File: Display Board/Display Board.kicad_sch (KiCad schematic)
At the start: 12 parts, among them J1 Display 1, J10 Display 1, J2 Display 2, J20 Display 2, J3 Control Board, J4 Top LED

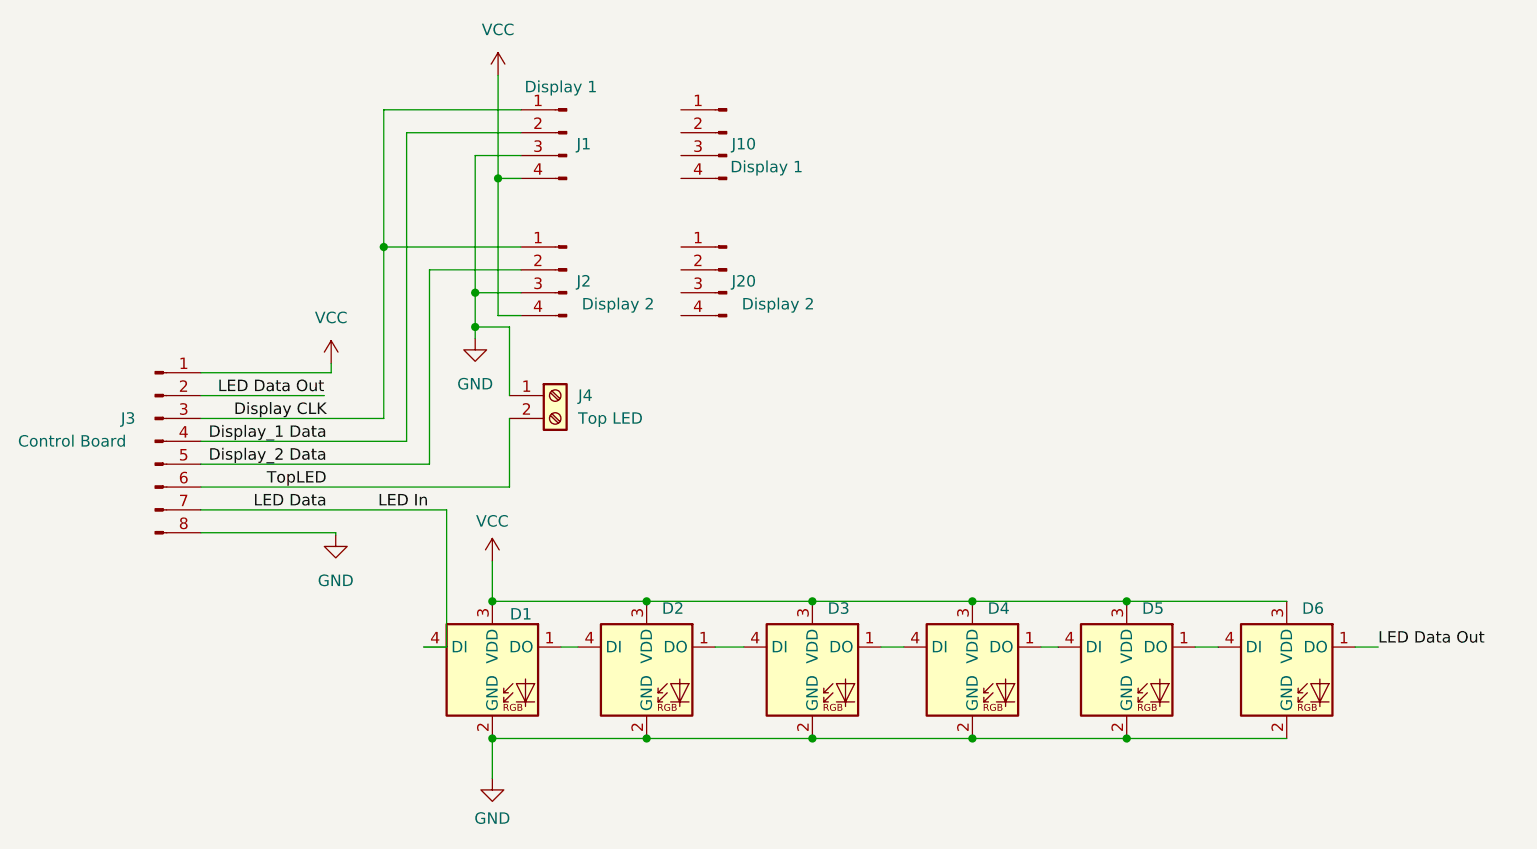
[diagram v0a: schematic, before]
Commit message: working on display board and mounting
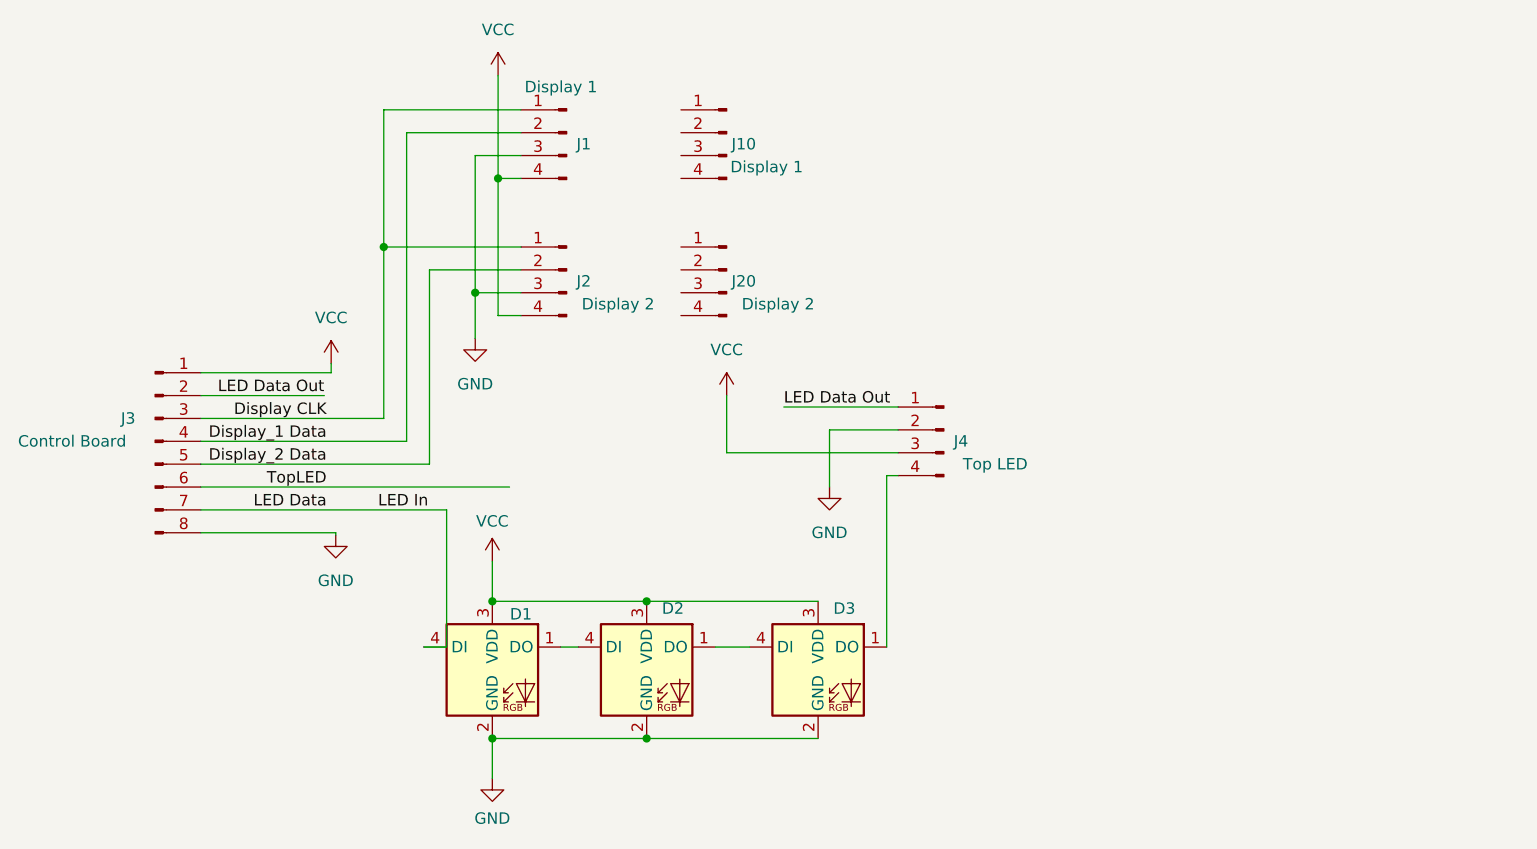
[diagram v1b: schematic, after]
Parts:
- removed D4, D5, D6: APA-106-F5, LED_THT:LED_D5.0mm-4_RGB, symbol LED:APA-106-F5
- removed J4: Top LED, TerminalBlock:TerminalBlock_Altech_AK300-2_P5.00mm, symbol Connector:Screw_Terminal_01x02
- added J4: Top LED, Connector_PinHeader_2.00mm:PinHeader_1x04_P2.00mm_Vertical, symbol Connector:Conn_01x04_Pin
- J1, J10, J2, J20: footprint Connector_PinHeader_2.00mm:PinHeader_1x04_P2.00mm_Vertical -> Connector_PinHeader_2.54mm:PinHeader_1x04_P2.54mm_Vertical
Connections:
- net GND: now also J4.2 (Pin_2)
- net LED Data Out: now also J4.1 (Pin_1)
- net VCC: now also J4.3 (Pin_3)
- net at D3.1 (DO): now also J4.4 (Pin_4)
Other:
- moved on the sheet: D3

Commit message: update display board with mounting holes and copper pour
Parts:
- added J5: Flash Enable, Connector_PinHeader_2.54mm:PinHeader_1x02_P2.54mm_Vertical, symbol Connector_Generic:Conn_01x02
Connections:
- net Display_1 Data: now also J5.2 (Pin_2); no longer J1.2 (Pin_2)
- new net: J1.2 (Pin_2), J5.1 (Pin_1)
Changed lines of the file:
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@@
+    (stroke (width 0) (type default))
+  )
+  (wire (pts (xy 69.85 34.29) (xy 76.2 34.29))
     (stroke (width 0) (type default))
   )
@@
     (stroke (width 0) (type default))
   )
-  (wire (pts (xy 76.2 66.04) (xy 76.2 31.75))
-    (stroke (width 0) (type default))
-  )
   (wire (pts (xy 88.9 49.53) (xy 83.82 49.53))
     (stroke (width 0) (type default))
@@
     (stroke (width 0) (type default))
   )
+  (wire (pts (xy 76.2 66.04) (xy 76.2 34.29))
+    (stroke (width 0) (type default))
+  )
   (wire (pts (xy 73.66 44.45) (xy 73.66 29.21))
     (stroke (width 0) (type default))
@@
     (stroke (width 0) (type default))
   )
-  (wire (pts (xy 76.2 31.75) (xy 88.9 31.75))
+  (wire (pts (xy 69.85 31.75) (xy 88.9 31.75))
     (stroke (width 0) (type default))
   )
@@
   (wire (pts (xy 93.345 88.9) (xy 95.25 88.9))
     (stroke (width 0) (type default))
+  )
+  (text_box "Remove jumper to enable flash"
+    (at 48.26 35.56 0) (size 15.24 7.62)
+    (stroke (width 0) (type default))
+    (fill (type none))
+    (effects (font (size 1.27 1.27)) (justify left top))
   )
   (label "Display CLK" (at 67.31 63.5 180) (fields_autoplaced)
@@
     )
   )
+  (symbol (lib_id "Connector_Generic:Conn_01x02") (at 64.77 31.75 0) (mirror y) (unit 1)
+    (in_bom yes) (on_board yes) (dnp no)
+    (property "Reference" "J5" (at 62.23 31.75 0)
+      (effects (font (size 1.27 1.27)) (justify left))
+    )
+    (property "Value" "Flash Enable" (at 62.23 34.29 0)
+      (effects (font (size 1.27 1.27)) (justify left))
+    )
+    (property "Footprint" "Connector_PinHeader_2.54mm:PinHeader_1x02_P2.54mm_Vertical" (at 64.77 31.75 0)
+      (effects (font (size 1.27 1.27)) hide)
+    )
+    (property "Datasheet" "~" (at 64.77 31.75 0)
+      (effects (font (size 1.27 1.27)) hide)
+    )
+    (pin "1")
+    (pin "2")
+    (instances
+      (project "Display Board"
+        (path "/9233c679-66ad-4040-97da-acde908139b3"
+          (reference "J5") (unit 1)
+        )
+      )
+    )
+  )
   (symbol (lib_id "Connector:Conn_01x04_Pin") (at 111.76 46.99 0) (mirror y) (unit 1)
     (in_bom yes) (on_board yes) (dnp no)
@@
     )
   )
-  (symbol (lib_id "power:VCC") (at 86.36 25.4 0) (mirror y) (unit 1)
-    (in_bom yes) (on_board yes) (dnp no) (fields_autoplaced)
+  (symbol (lib_id "power:VCC") (at 86.36 25.4 0) (unit 1)
+    (in_bom yes) (on_board yes) (dnp no)
     (property "Reference" "#PWR05" (at 86.36 29.21 0)
       (effects (font (size 1.27 1.27)) hide)
